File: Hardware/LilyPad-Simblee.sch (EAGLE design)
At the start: 36 parts, among them U1 MIC5219 3.3V, U2 MCP73831, U3 RFD77101

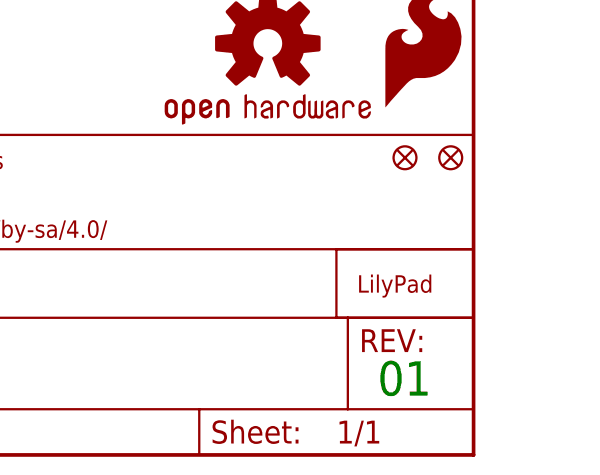
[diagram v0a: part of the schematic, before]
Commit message: Fixed QC feedback issues.
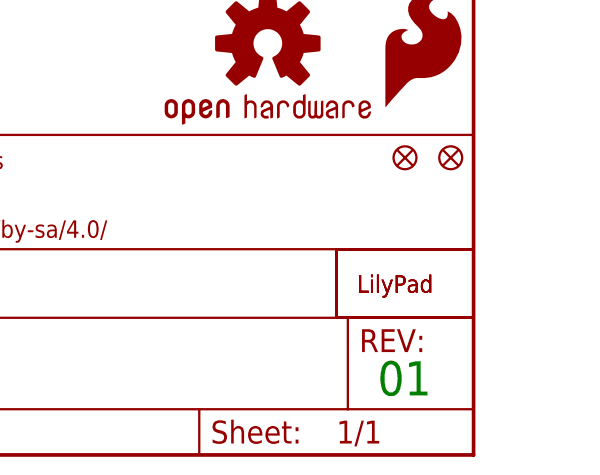
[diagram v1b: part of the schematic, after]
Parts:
- added U$2: LOGO-LPLP, LilyPad-Wearables:LOGO-LPLP
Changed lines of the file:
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@@
 <part name="FID2" library="SparkFun-Aesthetics" deviceset="FIDUCIAL" device="UFIDUCIAL"/>
 <part name="U$1" library="LilyPad-Wearables" deviceset="LOGO-LP" device="L"/>
+<part name="U$2" library="LilyPad-Wearables" deviceset="LOGO-LP" device="LP"/>
 </parts>
 <sheets>
@@
 <instance part="FID2" gate="G$1" x="241.3" y="33.02"/>
 <instance part="U$1" gate="G$1" x="236.22" y="17.78"/>
+<instance part="U$2" gate="G$1" x="236.22" y="17.78"/>
 </instances>
 <busses>

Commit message: Necessary changes for reds. Submitting for QC review
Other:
- note added: "10"
- note removed: "01"
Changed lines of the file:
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@@
 <text x="17.78" y="10.16" size="1.778" layer="95">L. Buechley</text>
 <text x="17.78" y="7.62" size="1.778" layer="95">N. Seidle</text>
-<text x="238.252" y="6.604" size="3.81" layer="91" font="vector">01</text>
+<text x="238.252" y="6.604" size="3.81" layer="91" font="vector">10</text>
 <text x="165.608" y="6.858" size="3.81" layer="91" font="vector">Mike Hord</text>
 <wire x1="0" y1="116.84" x2="147.32" y2="116.84" width="0.1524" layer="97" style="shortdash"/>

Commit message: Rep D8 w D6, add pour to antenna area, pour to top
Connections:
- removed net D8: A4/18.1, U3.P0.08
- new net D6: A4/18.1, U3.P0.06/AREF1/AIN7
- new net ISO_PAD: U3.GND@1, U3.GND@2, U3.GND@4
- net GND: no longer U3.GND@1, U3.GND@2, U3.GND@4
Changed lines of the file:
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@@
 <wire x1="48.26" y1="60.96" x2="48.26" y2="93.98" width="0.1524" layer="91"/>
 <junction x="48.26" y="60.96"/>
-<pinref part="U3" gate="G$1" pin="GND@1"/>
-<wire x1="48.26" y1="93.98" x2="48.26" y2="99.06" width="0.1524" layer="91"/>
-<wire x1="48.26" y1="99.06" x2="48.26" y2="104.14" width="0.1524" layer="91"/>
-<wire x1="48.26" y1="104.14" x2="48.26" y2="106.68" width="0.1524" layer="91"/>
-<wire x1="48.26" y1="106.68" x2="50.8" y2="106.68" width="0.1524" layer="91"/>
-<pinref part="U3" gate="G$1" pin="GND@2"/>
-<wire x1="50.8" y1="104.14" x2="48.26" y2="104.14" width="0.1524" layer="91"/>
-<junction x="48.26" y="104.14"/>
-<pinref part="U3" gate="G$1" pin="GND@4"/>
-<wire x1="50.8" y1="99.06" x2="48.26" y2="99.06" width="0.1524" layer="91"/>
-<junction x="48.26" y="99.06"/>
 <pinref part="U3" gate="G$1" pin="GND@6"/>
 <wire x1="50.8" y1="93.98" x2="48.26" y2="93.98" width="0.1524" layer="91"/>
-<junction x="48.26" y="93.98"/>
 </segment>
 <segment>
@@
 </segment>
 </net>
-<net name="D8" class="0">
-<segment>
-<pinref part="U3" gate="G$1" pin="P0.08"/>
-<wire x1="71.12" y1="43.18" x2="71.12" y2="15.24" width="0.1524" layer="91"/>
-<wire x1="71.12" y1="15.24" x2="83.82" y2="15.24" width="0.1524" layer="91"/>
-<label x="83.82" y="15.24" size="1.27" layer="95" xref="yes"/>
-</segment>
+<net name="D9" class="0">
+<segment>
+<pinref part="U3" gate="G$1" pin="P0.09"/>
+<wire x1="50.8" y1="63.5" x2="40.64" y2="63.5" width="0.1524" layer="91"/>
+<label x="40.64" y="63.5" size="1.27" layer="95" rot="R180" xref="yes"/>
+</segment>
+<segment>
+<pinref part="U$4" gate="G$1" pin="1"/>
+<wire x1="185.42" y1="66.04" x2="182.88" y2="66.04" width="0.1524" layer="91"/>
+<label x="182.88" y="66.04" size="1.27" layer="95" rot="R180" xref="yes"/>
+</segment>
+</net>
+<net name="D11" class="0">
+<segment>
+<pinref part="U3" gate="G$1" pin="P0.11"/>
+<wire x1="50.8" y1="66.04" x2="40.64" y2="66.04" width="0.1524" layer="91"/>
+<label x="40.64" y="66.04" size="1.27" layer="95" rot="R180" xref="yes"/>
+</segment>
+<segment>
+<pinref part="U$45" gate="G$1" pin="1"/>
+<wire x1="185.42" y1="68.58" x2="182.88" y2="68.58" width="0.1524" layer="91"/>
+<label x="182.88" y="68.58" size="1.27" layer="95" rot="R180" xref="yes"/>
+</segment>
+</net>
+<net name="D12" class="0">
+<segment>
+<pinref part="U3" gate="G$1" pin="P0.12"/>
+<wire x1="50.8" y1="68.58" x2="40.64" y2="68.58" width="0.1524" layer="91"/>
+<label x="40.64" y="68.58" size="1.27" layer="95" rot="R180" xref="yes"/>
+</segment>
+<segment>
+<pinref part="U$37" gate="G$1" pin="1"/>
+<wire x1="185.42" y1="71.12" x2="182.88" y2="71.12" width="0.1524" layer="91"/>
+<label x="182.88" y="71.12" size="1.27" layer="95" rot="R180" xref="yes"/>
+</segment>
+</net>
+<net name="D15" class="0">
+<segment>
+<pinref part="U3" gate="G$1" pin="P0.15"/>
+<wire x1="50.8" y1="71.12" x2="40.64" y2="71.12" width="0.1524" layer="91"/>
+<label x="40.64" y="71.12" size="1.27" layer="95" rot="R180" xref="yes"/>
+</segment>
+<segment>
+<pinref part="U$35" gate="G$1" pin="1"/>
+<wire x1="185.42" y1="73.66" x2="182.88" y2="73.66" width="0.1524" layer="91"/>
+<label x="182.88" y="73.66" size="1.27" layer="95" rot="R180" xref="yes"/>
+</segment>
+</net>
+<net name="D6" class="0">
 <segment>
 <pinref part="A4/18" gate="G$1" pin="1"/>
@@
 <label x="182.88" y="63.5" size="1.27" layer="95" rot="R180" xref="yes"/>
 </segment>
-</net>
-<net name="D9" class="0">
-<segment>
-<pinref part="U3" gate="G$1" pin="P0.09"/>
-<wire x1="50.8" y1="63.5" x2="40.64" y2="63.5" width="0.1524" layer="91"/>
-<label x="40.64" y="63.5" size="1.27" layer="95" rot="R180" xref="yes"/>
-</segment>
-<segment>
-<pinref part="U$4" gate="G$1" pin="1"/>
-<wire x1="185.42" y1="66.04" x2="182.88" y2="66.04" width="0.1524" layer="91"/>
-<label x="182.88" y="66.04" size="1.27" layer="95" rot="R180" xref="yes"/>
-</segment>
-</net>
-<net name="D11" class="0">
-<segment>
-<pinref part="U3" gate="G$1" pin="P0.11"/>
-<wire x1="50.8" y1="66.04" x2="40.64" y2="66.04" width="0.1524" layer="91"/>
-<label x="40.64" y="66.04" size="1.27" layer="95" rot="R180" xref="yes"/>
-</segment>
-<segment>
-<pinref part="U$45" gate="G$1" pin="1"/>
-<wire x1="185.42" y1="68.58" x2="182.88" y2="68.58" width="0.1524" layer="91"/>
-<label x="182.88" y="68.58" size="1.27" layer="95" rot="R180" xref="yes"/>
-</segment>
-</net>
-<net name="D12" class="0">
-<segment>
-<pinref part="U3" gate="G$1" pin="P0.12"/>
-<wire x1="50.8" y1="68.58" x2="40.64" y2="68.58" width="0.1524" layer="91"/>
-<label x="40.64" y="68.58" size="1.27" layer="95" rot="R180" xref="yes"/>
-</segment>
-<segment>
-<pinref part="U$37" gate="G$1" pin="1"/>
-<wire x1="185.42" y1="71.12" x2="182.88" y2="71.12" width="0.1524" layer="91"/>
-<label x="182.88" y="71.12" size="1.27" layer="95" rot="R180" xref="yes"/>
-</segment>
-</net>
-<net name="D15" class="0">
-<segment>
-<pinref part="U3" gate="G$1" pin="P0.15"/>
-<wire x1="50.8" y1="71.12" x2="40.64" y2="71.12" width="0.1524" layer="91"/>
-<label x="40.64" y="71.12" size="1.27" layer="95" rot="R180" xref="yes"/>
-</segment>
-<segment>
-<pinref part="U$35" gate="G$1" pin="1"/>
-<wire x1="185.42" y1="73.66" x2="182.88" y2="73.66" width="0.1524" layer="91"/>
-<label x="182.88" y="73.66" size="1.27" layer="95" rot="R180" xref="yes"/>
-</segment>
-</net>
+<segment>
+<pinref part="U3" gate="G$1" pin="P0.06/AREF1/AIN7"/>
+<wire x1="114.3" y1="63.5" x2="116.84" y2="63.5" width="0.1524" layer="91"/>
+<label x="116.84" y="63.5" size="1.27" layer="95" xref="yes"/>
+</segment>
+</net>
+<net name="ISO_PAD" class="0">
+<segment>
+<pinref part="U3" gate="G$1" pin="GND@1"/>
+<wire x1="48.26" y1="106.68" x2="50.8" y2="106.68" width="0.1524" layer="91"/>
+<wire x1="48.26" y1="104.14" x2="48.26" y2="106.68" width="0.1524" layer="91"/>
+<pinref part="U3" gate="G$1" pin="GND@2"/>
+<wire x1="50.8" y1="104.14" x2="48.26" y2="104.14" width="0.1524" layer="91"/>
+<junction x="48.26" y="104.14"/>
+<wire x1="48.26" y1="99.06" x2="48.26" y2="104.14" width="0.1524" layer="91"/>
+<pinref part="U3" gate="G$1" pin="GND@4"/>
+<wire x1="50.8" y1="99.06" x2="48.26" y2="99.06" width="0.1524" layer="91"/>
+<wire x1="48.26" y1="106.68" x2="48.26" y2="114.3" width="0.1524" layer="91"/>
+<junction x="48.26" y="106.68"/>
+<wire x1="48.26" y1="114.3" x2="53.34" y2="114.3" width="0.1524" layer="91"/>
+<label x="53.34" y="114.3" size="1.27" layer="95" xref="yes"/>
+</segment>
+</net>

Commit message: Fix some QC review issues
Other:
- note added: "11"
- note removed: "10"
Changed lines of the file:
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@@
 <text x="17.78" y="10.16" size="1.778" layer="95">L. Buechley</text>
 <text x="17.78" y="7.62" size="1.778" layer="95">N. Seidle</text>
-<text x="238.252" y="6.604" size="3.81" layer="91" font="vector">10</text>
+<text x="238.252" y="6.604" size="3.81" layer="91" font="vector">11</text>
 <text x="165.608" y="6.858" size="3.81" layer="91" font="vector">Mike Hord</text>
 <wire x1="0" y1="116.84" x2="147.32" y2="116.84" width="0.1524" layer="97" style="shortdash"/>

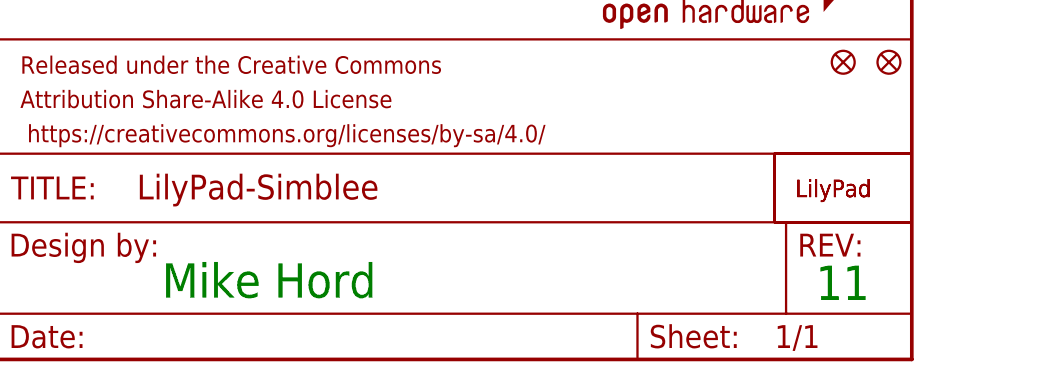
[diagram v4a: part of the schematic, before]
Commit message: Chg to V12, reduce paste on GND pads to 12.5%
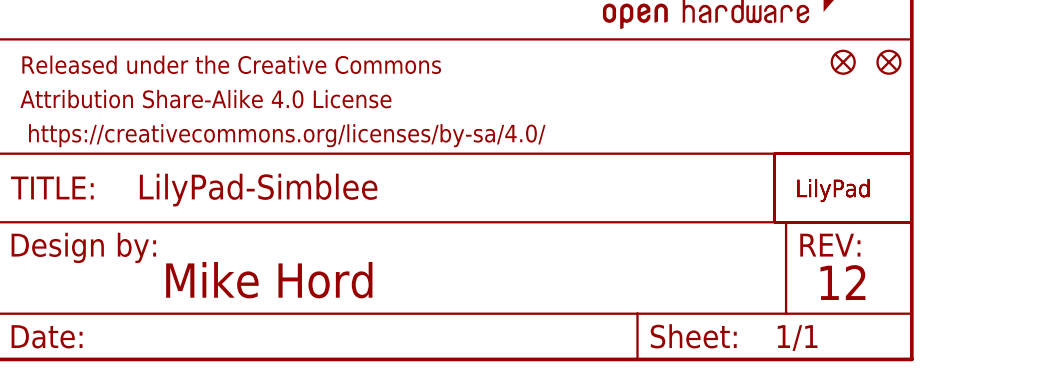
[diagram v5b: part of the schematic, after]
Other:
- note added: "12"
- note removed: "11"
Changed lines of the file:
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@@
 <text x="17.78" y="10.16" size="1.778" layer="95">L. Buechley</text>
 <text x="17.78" y="7.62" size="1.778" layer="95">N. Seidle</text>
-<text x="238.252" y="6.604" size="3.81" layer="91" font="vector">11</text>
-<text x="165.608" y="6.858" size="3.81" layer="91" font="vector">Mike Hord</text>
+<text x="238.252" y="6.604" size="3.81" layer="94" font="vector">12</text>
+<text x="165.608" y="6.858" size="3.81" layer="94" font="vector">Mike Hord</text>
 <wire x1="0" y1="116.84" x2="147.32" y2="116.84" width="0.1524" layer="97" style="shortdash"/>
 <wire x1="147.32" y1="116.84" x2="147.32" y2="81.28" width="0.1524" layer="97" style="shortdash"/>

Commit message: Release
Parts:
- U1: value MIC5219 3.3V -> ADP160; device SparkFun-PowerIC:V_REG_MIC52193.3V -> SparkFun-PowerIC:ADP160
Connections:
- net 3.3V: now also U1.VOUT; no longer U1.OUT
- net 5V: now also U1.VIN; no longer U1.IN
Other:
- moved on the sheet: C2
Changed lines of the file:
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@@
 <part name="A5/19" library="LilyPad-Wearables" deviceset="SEWTAP" device="9"/>
 <part name="U$4" library="LilyPad-Wearables" deviceset="SEWTAP" device="9"/>
-<part name="GND3" library="SparkFun" deviceset="GND" device=""/>
 <part name="GND9" library="SparkFun" deviceset="GND" device=""/>
 <part name="JP2" library="SparkFun-Connectors" deviceset="ARDUINO_SERIAL_PROGRAM" device="SMD">
@@
 <part name="SUPPLY9" library="SparkFun-Aesthetics" deviceset="V_BATT" device=""/>
 <part name="C2" library="SparkFun-Capacitors" deviceset="2.2UF-10V-20%(0603)" device="" value="2.2uF"/>
-<part name="U1" library="SparkFun-PowerIC" deviceset="V_REG_MIC5219" device="3.3V" value="MIC5219 3.3V"/>
 <part name="D1" library="SparkFun-DiscreteSemi" deviceset="BAT20JFILM" device="" value="BAT20JFILM"/>
 <part name="SUPPLY10" library="SparkFun-Aesthetics" deviceset="5V" device=""/>
@@
 <part name="U$1" library="LilyPad-Wearables" deviceset="LOGO-LP" device="L"/>
 <part name="U$2" library="LilyPad-Wearables" deviceset="LOGO-LP" device="LP"/>
+<part name="U1" library="SparkFun-PowerIC" deviceset="ADP160" device="" value="ADP160"/>
 </parts>
 <sheets>
@@
 <instance part="A5/19" gate="G$1" x="187.96" y="58.42" smashed="yes"/>
 <instance part="U$4" gate="G$1" x="187.96" y="66.04" smashed="yes"/>
-<instance part="GND3" gate="1" x="185.42" y="154.94"/>
 <instance part="GND9" gate="1" x="48.26" y="55.88"/>
 <instance part="JP2" gate="G$1" x="175.26" y="101.6" rot="R180">
@@
 <instance part="SUPPLY1" gate="G$1" x="30.48" y="104.14"/>
 <instance part="SUPPLY2" gate="G$1" x="40.64" y="99.06"/>
-<instance part="GND4" gate="1" x="215.9" y="147.32"/>
-<instance part="SUPPLY3" gate="G$1" x="213.36" y="167.64"/>
+<instance part="GND4" gate="1" x="226.06" y="147.32"/>
+<instance part="SUPPLY3" gate="G$1" x="223.52" y="167.64"/>
 <instance part="SUPPLY4" gate="G$1" x="15.24" y="43.18"/>
 <instance part="SUPPLY6" gate="G$1" x="167.64" y="109.22"/>
@@
 <instance part="SUPPLY8" gate="G$1" x="63.5" y="149.86"/>
 <instance part="SUPPLY9" gate="G$1" x="149.86" y="167.64"/>
-<instance part="C2" gate="G$1" x="215.9" y="157.48"/>
-<instance part="U1" gate="G$1" x="203.2" y="160.02"/>
+<instance part="C2" gate="G$1" x="226.06" y="157.48"/>
 <instance part="D1" gate="G$1" x="165.1" y="165.1"/>
 <instance part="SUPPLY10" gate="G$1" x="185.42" y="167.64"/>
@@
 <instance part="U$1" gate="G$1" x="236.22" y="17.78"/>
 <instance part="U$2" gate="G$1" x="236.22" y="17.78"/>
+<instance part="U1" gate="G$1" x="205.74" y="162.56"/>
 </instances>
 <busses>
@@
 </segment>
 <segment>
-<pinref part="GND3" gate="1" pin="GND"/>
-<wire x1="185.42" y1="157.48" x2="185.42" y2="160.02" width="0.1524" layer="91"/>
-<pinref part="U1" gate="G$1" pin="GND"/>
-<wire x1="185.42" y1="160.02" x2="193.04" y2="160.02" width="0.1524" layer="91"/>
-</segment>
-<segment>
 <pinref part="GND5" gate="1" pin="GND"/>
 <wire x1="170.18" y1="132.08" x2="170.18" y2="134.62" width="0.1524" layer="91"/>
@@
 <pinref part="GND4" gate="1" pin="GND"/>
 <pinref part="C2" gate="G$1" pin="2"/>
-<wire x1="215.9" y1="149.86" x2="215.9" y2="154.94" width="0.1524" layer="91"/>
+<wire x1="226.06" y1="149.86" x2="226.06" y2="152.4" width="0.1524" layer="91"/>
+<wire x1="226.06" y1="152.4" x2="226.06" y2="154.94" width="0.1524" layer="91"/>
+<wire x1="220.98" y1="160.02" x2="220.98" y2="152.4" width="0.1524" layer="91"/>
+<wire x1="220.98" y1="152.4" x2="226.06" y2="152.4" width="0.1524" layer="91"/>
+<junction x="226.06" y="152.4"/>
+<pinref part="U1" gate="G$1" pin="GND"/>
+<wire x1="218.44" y1="160.02" x2="220.98" y2="160.02" width="0.1524" layer="91"/>
 </segment>
 <segment>
@@
 </segment>
 <segment>
-<pinref part="U1" gate="G$1" pin="OUT"/>
 <pinref part="SUPPLY3" gate="G$1" pin="3.3V"/>
-<wire x1="210.82" y1="165.1" x2="213.36" y2="165.1" width="0.1524" layer="91"/>
-<wire x1="213.36" y1="165.1" x2="213.36" y2="167.64" width="0.1524" layer="91"/>
+<wire x1="223.52" y1="165.1" x2="223.52" y2="167.64" width="0.1524" layer="91"/>
 <pinref part="C2" gate="G$1" pin="1"/>
-<wire x1="213.36" y1="165.1" x2="215.9" y2="165.1" width="0.1524" layer="91"/>
-<wire x1="215.9" y1="165.1" x2="215.9" y2="162.56" width="0.1524" layer="91"/>
-<junction x="213.36" y="165.1"/>
+<wire x1="223.52" y1="165.1" x2="226.06" y2="165.1" width="0.1524" layer="91"/>
+<wire x1="226.06" y1="165.1" x2="226.06" y2="162.56" width="0.1524" layer="91"/>
+<pinref part="U1" gate="G$1" pin="VOUT"/>
+<wire x1="218.44" y1="165.1" x2="223.52" y2="165.1" width="0.1524" layer="91"/>
+<junction x="223.52" y="165.1"/>
 </segment>
 <segment>
@@
 <segment>
 <wire x1="193.04" y1="165.1" x2="185.42" y2="165.1" width="0.1524" layer="91"/>
-<pinref part="U1" gate="G$1" pin="IN"/>
 <pinref part="D1" gate="G$1" pin="C"/>
 <wire x1="167.64" y1="165.1" x2="185.42" y2="165.1" width="0.1524" layer="91"/>
@@
 <wire x1="185.42" y1="167.64" x2="185.42" y2="165.1" width="0.1524" layer="91"/>
 <junction x="185.42" y="165.1"/>
+<pinref part="U1" gate="G$1" pin="VIN"/>
 </segment>
 <segment>
@@
 <pinref part="S2" gate="G$1" pin="2"/>
 <wire x1="185.42" y1="137.16" x2="190.5" y2="137.16" width="0.1524" layer="91"/>
-<wire x1="190.5" y1="137.16" x2="190.5" y2="154.94" width="0.1524" layer="91"/>
+<wire x1="190.5" y1="137.16" x2="190.5" y2="160.02" width="0.1524" layer="91"/>
 <pinref part="U1" gate="G$1" pin="EN"/>
-<wire x1="190.5" y1="154.94" x2="193.04" y2="154.94" width="0.1524" layer="91"/>
-</segment>
-</net>
+<wire x1="190.5" y1="160.02" x2="193.04" y2="160.02" width="0.1524" layer="91"/>
+</segment>
+</net>
